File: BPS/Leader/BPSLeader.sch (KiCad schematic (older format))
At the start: 21 parts, among them J1 SWD, J13 CAN Analyzer, J5 SPI Analyzer, SW1 B3SL-1002P, U1 STM32F413RHTx, Y1 8M

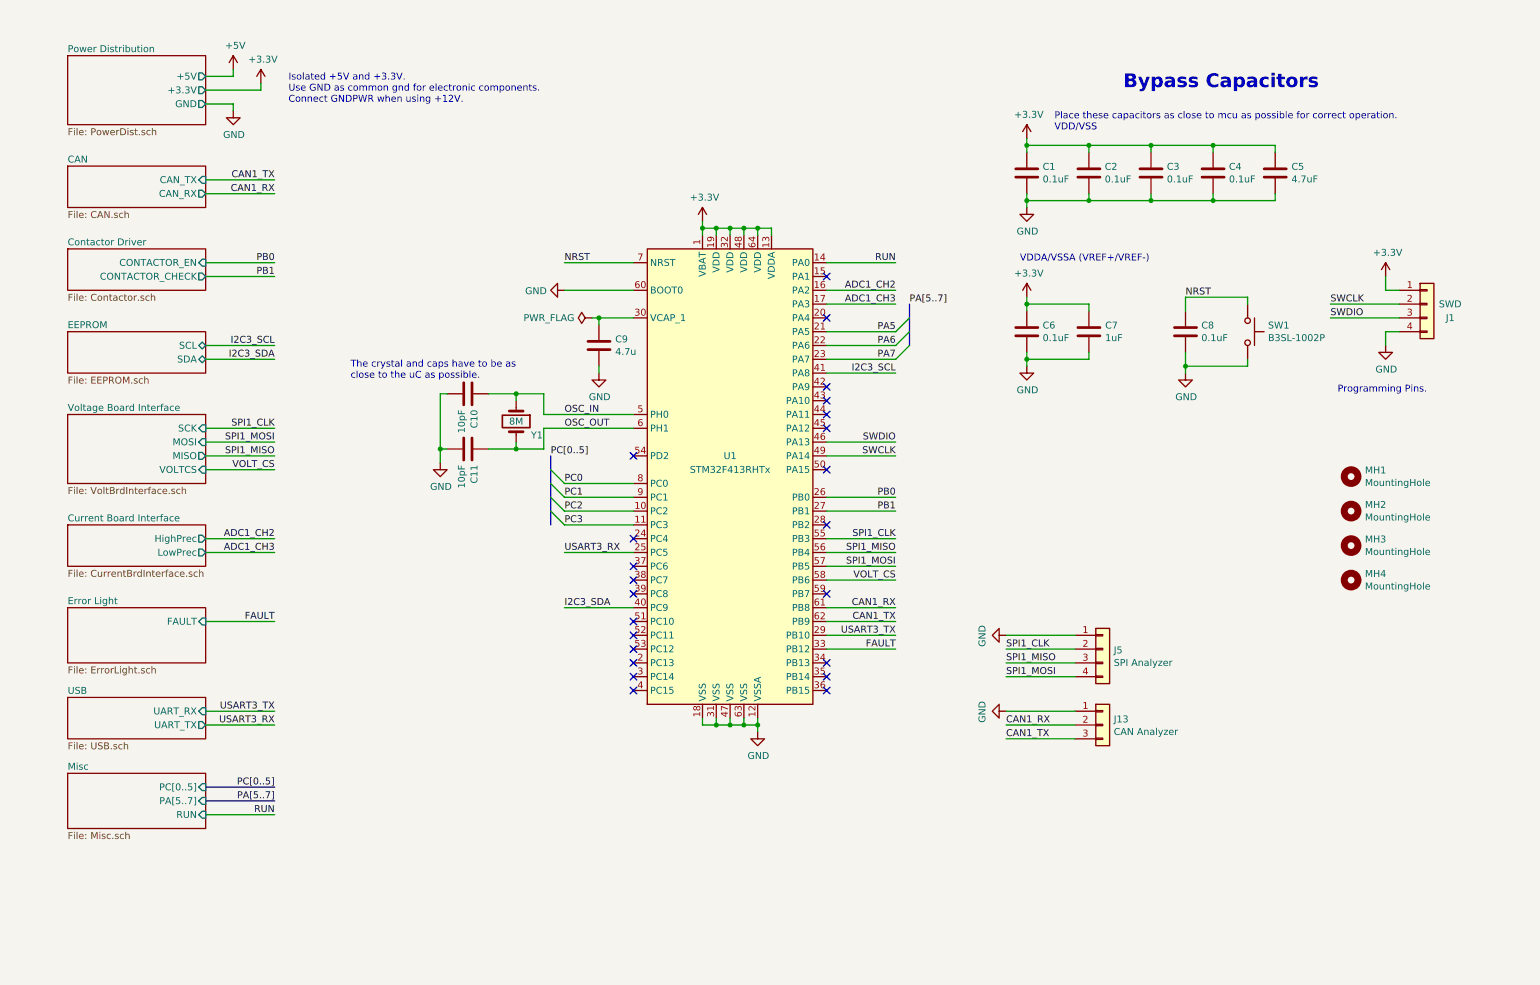
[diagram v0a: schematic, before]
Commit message: Leader board (#42)
* Creates fan brd interface schematics and updates symbols/footprints related to the leader board

* Finishes schematics for bps leader board

* Renames bps master to bps leader:

* Places most components of leader board in their respective locations with nothing traced

* Adds power planes

* Everything traced in leader board except for power circuitry

* Traces power components

* Finished leader board

* Simplifies dc-dc converter schematics

* Updates leader board, need to add comments

* Finishes new power circuitry tracing

* Adds version number to leader_board and creates schematics pdf

* Edits diode V2F22HM footprint to not have a copper cutout

* Adds copper cutout to transformer for isospi because ltc6820 datasheet recommended it

* Changes LTC6820 POL and PHA pins to +5V due to VIH and VIL parameters in datasheet

* Checks and make sure everything passes DRC

* Updates V2F22HM footprint to include polarity indicator on silkscreen

* Adds documents/pdfs to leader board

* Deletes errenous pdf

* Checks ERC/DRC one more time

* Updates LTC6820 symbol

* Removes previous current board interface hierachy sheet

* These twwo files were combined into SensorBrdInterface.sch
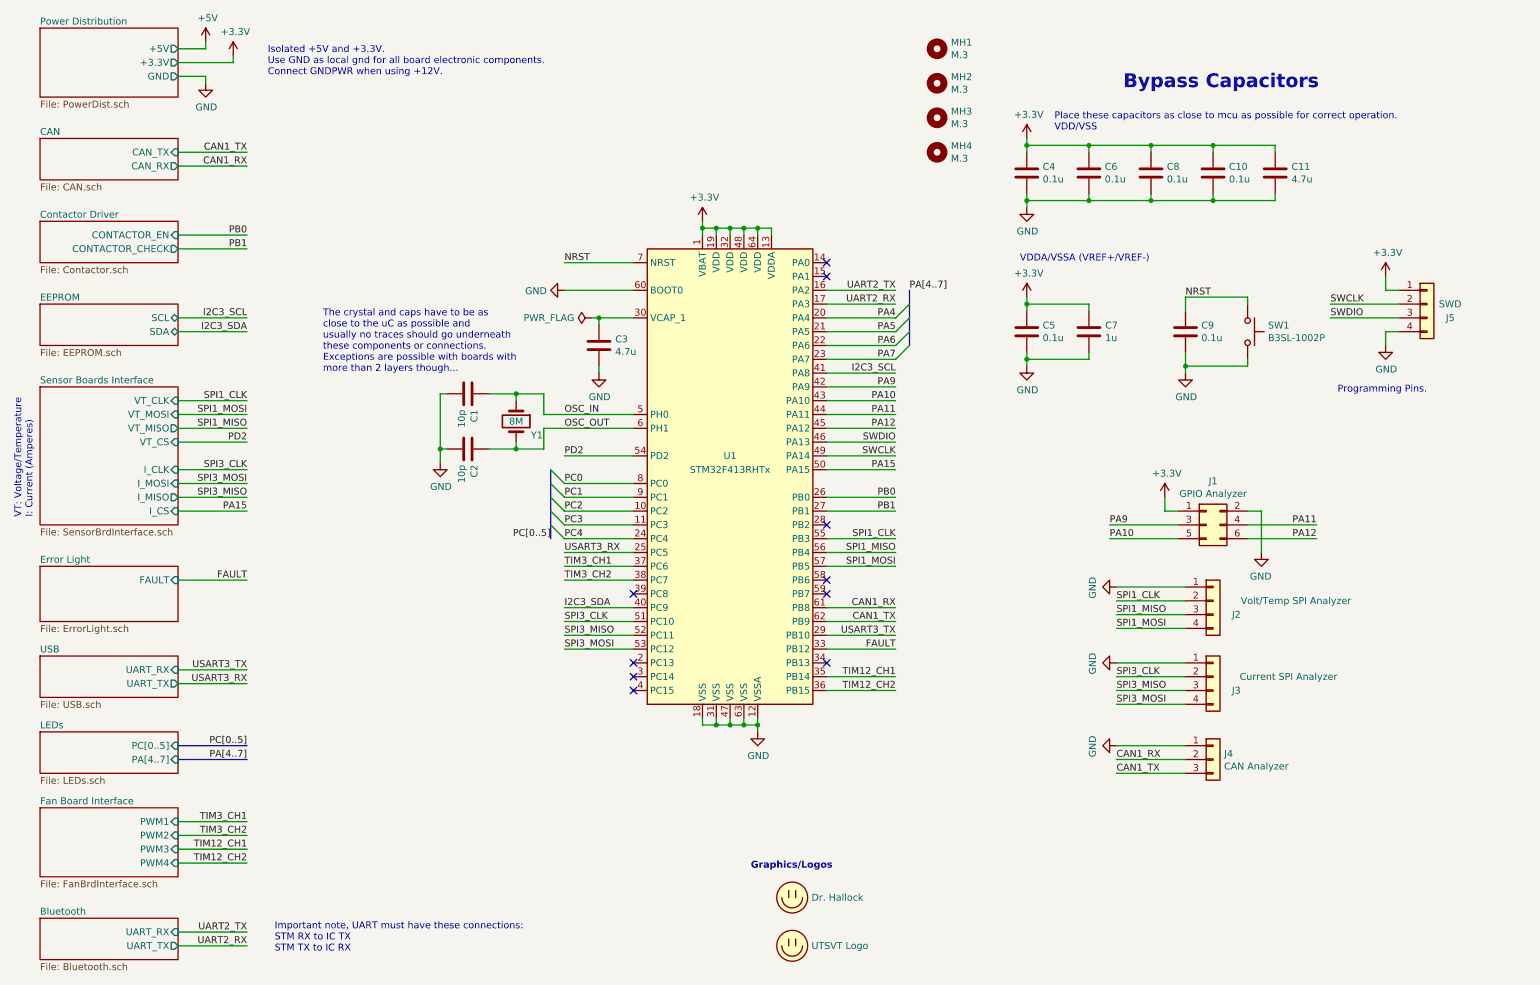
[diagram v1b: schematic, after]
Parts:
- removed J5: SPI Analyzer, Connector_PinHeader_2.54mm:PinHeader_1x04_P2.54mm_Vertical, symbol Connector_Generic:Conn_01x04
- added J1: GPIO Analyzer, Connector_PinHeader_2.54mm:PinHeader_2x03_P2.54mm_Vertical, symbol Connector_Generic:Conn_02x03_Odd_Even
- added J2: Volt/Temp SPI Analyzer, Connector_PinHeader_2.54mm:PinHeader_1x04_P2.54mm_Vertical, symbol Connector_Generic:Conn_01x04
- added J3: Current SPI Analyzer, Connector_PinHeader_2.54mm:PinHeader_1x04_P2.54mm_Vertical, symbol Connector_Generic:Conn_01x04
- added LOGO1: Dr. Hallock, UTSVT_Special:Hallock_Image_Small, symbol utsvt-misc:Logo_Placeholder
- added LOGO2: UTSVT Logo, UTSVT_Special:UTSVT_Logo_Symbol, symbol utsvt-misc:Logo_Placeholder
- C1: renamed from C10; value 10pF -> 10p
- C10: renamed from C4; value 0.1uF -> 0.1u
- C11: renamed from C5; value 4.7uF -> 4.7u
- C2: renamed from C11; value 10pF -> 10p
- C4: renamed from C1; value 0.1uF -> 0.1u
- C5: renamed from C6; value 0.1uF -> 0.1u
- C6: renamed from C2; value 0.1uF -> 0.1u
- C7: value 1uF -> 1u
- C8: renamed from C3; value 0.1uF -> 0.1u
- C9: renamed from C8; value 0.1uF -> 0.1u
- MH1, MH2, MH3, MH4: value MountingHole -> M.3
- renumbered C9 to C3, J13 to J4, J1 to J5
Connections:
- net +3V3: now also J1.1 (Pin_1)
- net GND: now also J1.2 (Pin_2), J2.1 (Pin_1), J3.1 (Pin_1)
- net SPI1_CLK: now also J2.2 (Pin_2)
- net SPI1_MISO: now also J2.3 (Pin_3)
- net SPI1_MOSI: now also J2.4 (Pin_4)
- net PA4: now reaches U1.20 (PA4)
- net PC4: now reaches U1.24 (PC4)
- net TIM12_CH1: now reaches U1.35 (PB14)
- net TIM12_CH2: now reaches U1.36 (PB15)
- net TIM3_CH1: now reaches U1.37 (PC6)
- net TIM3_CH2: now reaches U1.38 (PC7)
- net PA9: now reaches U1.42 (PA9)
- net PA9: now also J1.3 (Pin_3)
- net PA10: now reaches U1.43 (PA10)
- net PA10: now also J1.5 (Pin_5)
- net PA11: now reaches U1.44 (PA11)
- net PA11: now also J1.4 (Pin_4)
- net PA12: now reaches U1.45 (PA12)
- net PA12: now also J1.6 (Pin_6)
- net PA15: now reaches U1.50 (PA15)
- net SPI3_CLK: now reaches U1.51 (PC10)
- net SPI3_CLK: now also J3.2 (Pin_2)
- net SPI3_MISO: now reaches U1.52 (PC11)
- net SPI3_MISO: now also J3.3 (Pin_3)
- net SPI3_MOSI: now reaches U1.53 (PC12)
- net SPI3_MOSI: now also J3.4 (Pin_4)
- net PD2: now reaches U1.54 (PD2)
- net ADC1_CH2 renamed UART2_TX
- net ADC1_CH3 renamed UART2_RX
- net RUN: no longer names the net of U1.14 (PA0)
- net VOLT_CS: no longer names the net of U1.58 (PB6)
- no-connect marks 23 -> 10
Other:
- note added: "Graphics/Logos"
- note added: "Important note, UART must have these connections:\nSTM RX to IC TX\nSTM TX to IC RX"
- note added: "Isolated +5V and +3.3V.\nUse GND as local gnd for all board electronic components.\nConnect GNDPWR when using +12V."
- note added: "The crystal and caps have to be as \nclose to the uC as possible and\nusually no traces should go underneath\nthese components or connections.\nExceptions are possible with boards with\nmore than 2 layers though..."
- note added: "VT: Voltage/Temperature\nI: Current (Amperes)"
- note removed: "Isolated +5V and +3.3V.\nUse GND as common gnd for electronic components.\nConnect GNDPWR when using +12V."
- note removed: "The crystal and caps have to be as \nclose to the uC as possible."
- moved on the sheet: J4, MH1, MH2, MH3, MH4
